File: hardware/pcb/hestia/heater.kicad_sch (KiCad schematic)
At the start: 22 parts, among them Q1 FDS8876, SW2 SW_Push_Open, U10 INA826

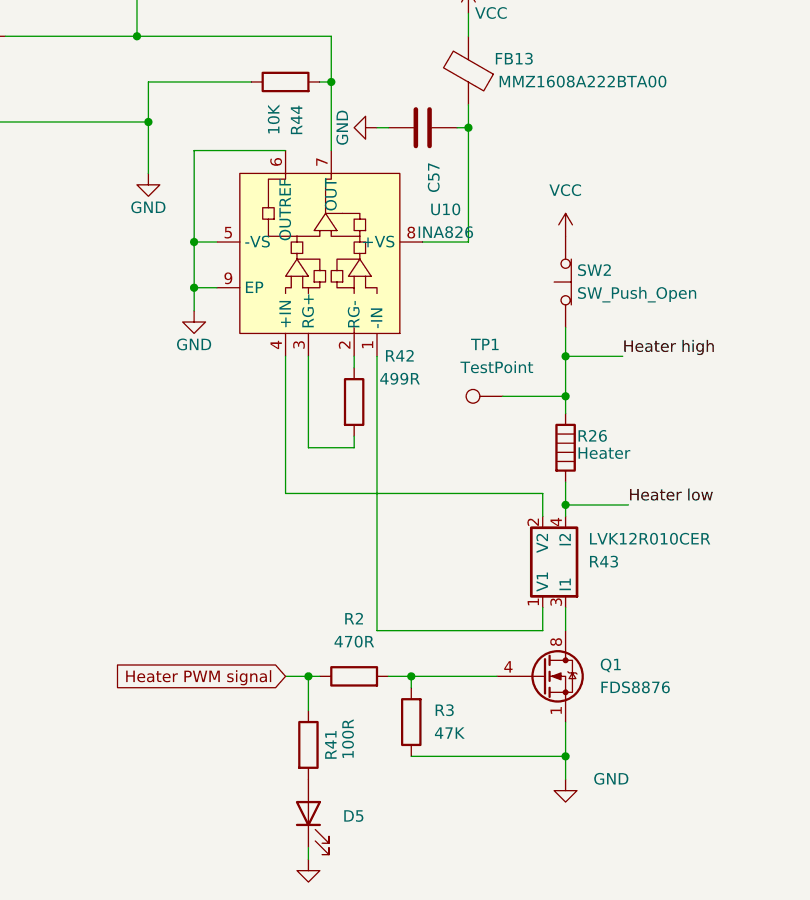
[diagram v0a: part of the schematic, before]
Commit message: pcb: disable undervoltage latch on 3.3V regulator
- replace C3 with 0R to connect LDELAY to GND
- update footprint on PCB
- fixes #18, fixes #25
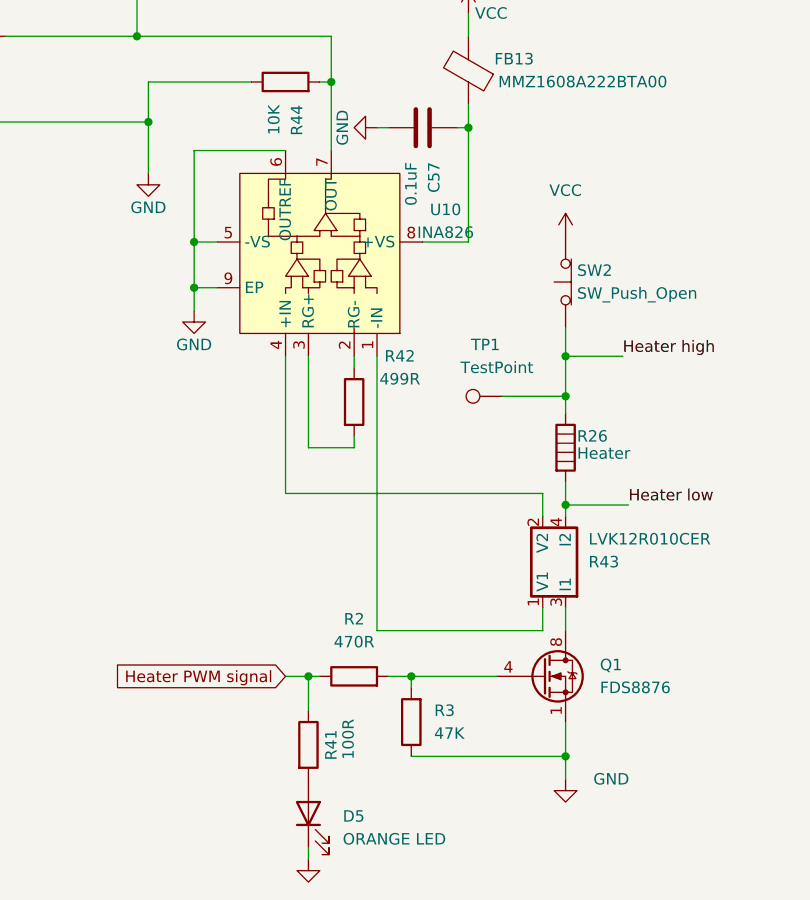
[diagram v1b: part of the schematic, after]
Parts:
- C57: value (none) -> 0.1uF; footprint (none) -> Capacitor_SMD:C_0603_1608Metric_Pad1.08x0.95mm_HandSolder
- D5: value (none) -> ORANGE LED; footprint (none) -> LED_SMD:LED_0805_2012Metric_Pad1.15x1.40mm_HandSolder
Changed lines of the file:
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@@
       (effects (font (size 1.27 1.27)) (justify right))
     )
-    (property "Value" "" (id 1) (at 104.775 140.6524 90)
+    (property "Value" "ORANGE LED" (id 1) (at 104.775 140.6524 90)
       (effects (font (size 1.27 1.27)) (justify right))
     )
-    (property "Footprint" "" (id 2) (at 100.965 137.795 0)
+    (property "Footprint" "LED_SMD:LED_0805_2012Metric_Pad1.15x1.40mm_HandSolder" (id 2) (at 100.965 137.795 0)
       (effects (font (size 1.27 1.27)) hide)
     )
@@
       (effects (font (size 1.27 1.27)) (justify left))
     )
-    (property "Value" "" (id 1) (at 112.3951 65.405 0)
+    (property "Value" "0.1uF" (id 1) (at 112.3951 65.405 0)
       (effects (font (size 1.27 1.27)) (justify left))
     )
-    (property "Footprint" "" (id 2) (at 109.855 62.5602 0)
+    (property "Footprint" "Capacitor_SMD:C_0603_1608Metric_Pad1.08x0.95mm_HandSolder" (id 2) (at 109.855 62.5602 0)
       (effects (font (size 1.27 1.27)) hide)
     )

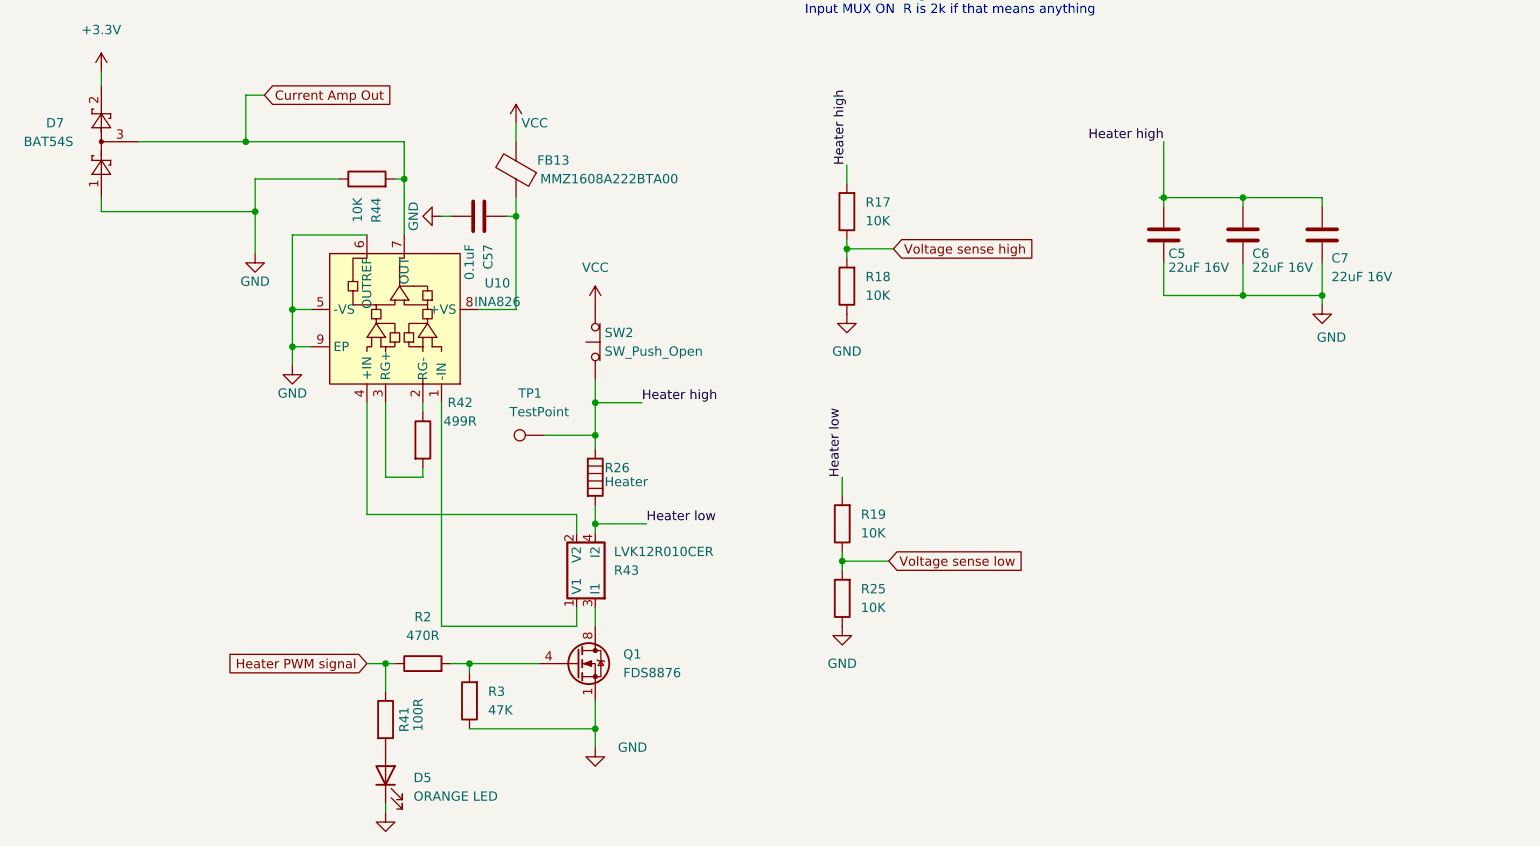
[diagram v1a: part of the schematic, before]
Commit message: change Y2 to 14.7456MHz because 7.3728MHz would have required the bigger size crystal pad. chose xtal load cap 12.5pf and 12pf for xtals. chose 20pf ext load caps to suit for C11,C12,C13,C14. Change D6 to FSV340AF - same family just 40V reverse voltage max rather than 30V reverse voltage max because FSV330AF was out of stock. Added some more digikey part numbers
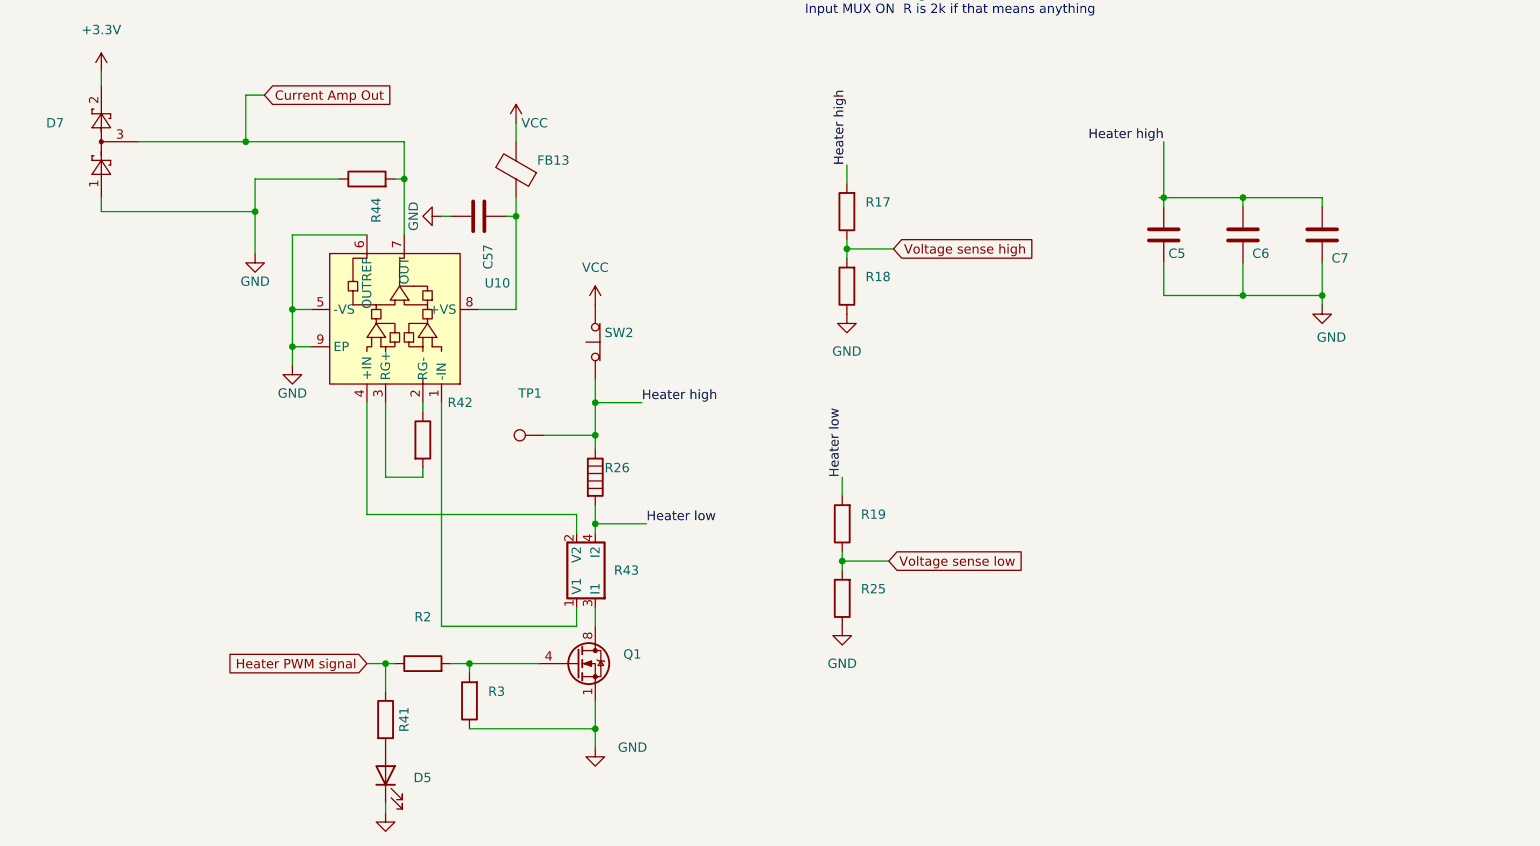
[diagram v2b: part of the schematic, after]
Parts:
- C5, C6, C7: value 22uF 16V -> (none); footprint Capacitor_SMD:C_1206_3216Metric -> (none)
- C57: value 0.1uF -> (none); footprint Capacitor_SMD:C_0603_1608Metric_Pad1.08x0.95mm_HandSolder -> (none)
- D5: value ORANGE LED -> (none); footprint LED_SMD:LED_0805_2012Metric_Pad1.15x1.40mm_HandSolder -> (none); Digikey Part (none) -> 475-2486-1-ND
- D7: value BAT54S -> (none); footprint Package_TO_SOT_SMD:SOT-23 -> (none)
- FB13: value MMZ1608A222BTA00 -> (none); footprint Resistor_SMD:R_0603_1608Metric_Pad0.98x0.95mm_HandSolder -> (none)
- Q1: value FDS8876 -> (none); footprint Package_SO:SOIC-8_3.9x4.9mm_P1.27mm -> (none)
- R17, R18, R19, R25, R44: value 10K -> (none); footprint Resistor_SMD:R_0603_1608Metric_Pad0.98x0.95mm_HandSolder -> (none)
- R2: value 470R -> (none); footprint Resistor_SMD:R_0603_1608Metric_Pad0.98x0.95mm_HandSolder -> (none)
- R26: value Heater -> (none); footprint NetTie:NetTie-2_SMD_Pad0.5mm -> (none)
- R3: value 47K -> (none); footprint Resistor_SMD:R_0603_1608Metric_Pad0.98x0.95mm_HandSolder -> (none)
- R41: value 100R -> (none); footprint Resistor_SMD:R_0603_1608Metric_Pad0.98x0.95mm_HandSolder -> (none)
- R42: value 499R -> (none); footprint Capacitor_SMD:C_0402_1005Metric -> (none)
- R43: value LVK12R010CER -> (none); footprint Hestia:LVK12R010CER -> (none)
- SW2: value SW_Push_Open -> (none); footprint Connector_PinHeader_2.54mm:PinHeader_1x02_P2.54mm_Vertical -> (none)
- TP1: value TestPoint -> (none); footprint TestPoint:TestPoint_Pad_2.0x2.0mm -> (none)
- U10: value INA826 -> (none); footprint Package_SON:WSON-8-1EP_3x3mm_P0.5mm_EP1.2x2mm -> (none)
